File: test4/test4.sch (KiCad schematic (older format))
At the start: 2 parts, among them U1 74LS245, U2 74LS245

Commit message: playing with schematic symbol editor
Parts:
- added U?: test1, symbol test1
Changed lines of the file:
@@
 LIBS:contrib
 LIBS:valves
+LIBS:test1
+LIBS:test4-cache
 EELAYER 25 0
 EELAYER END
@@
 	4950 5050 4950 4850
 Connection ~ 4950 4850
+$Comp
+L test1 U?
+U 1 1 5672C530
+P 7400 1600
+F 0 "U?" H 7400 1600 60  0000 C CNN
+F 1 "test1" H 7400 1600 60  0000 C CNN
+F 2 "" H 7400 1600 60  0000 C CNN
+F 3 "" H 7400 1600 60  0000 C CNN
+	1    7400 1600
+	1    0    0    -1
+$EndComp
 $EndSCHEMATC

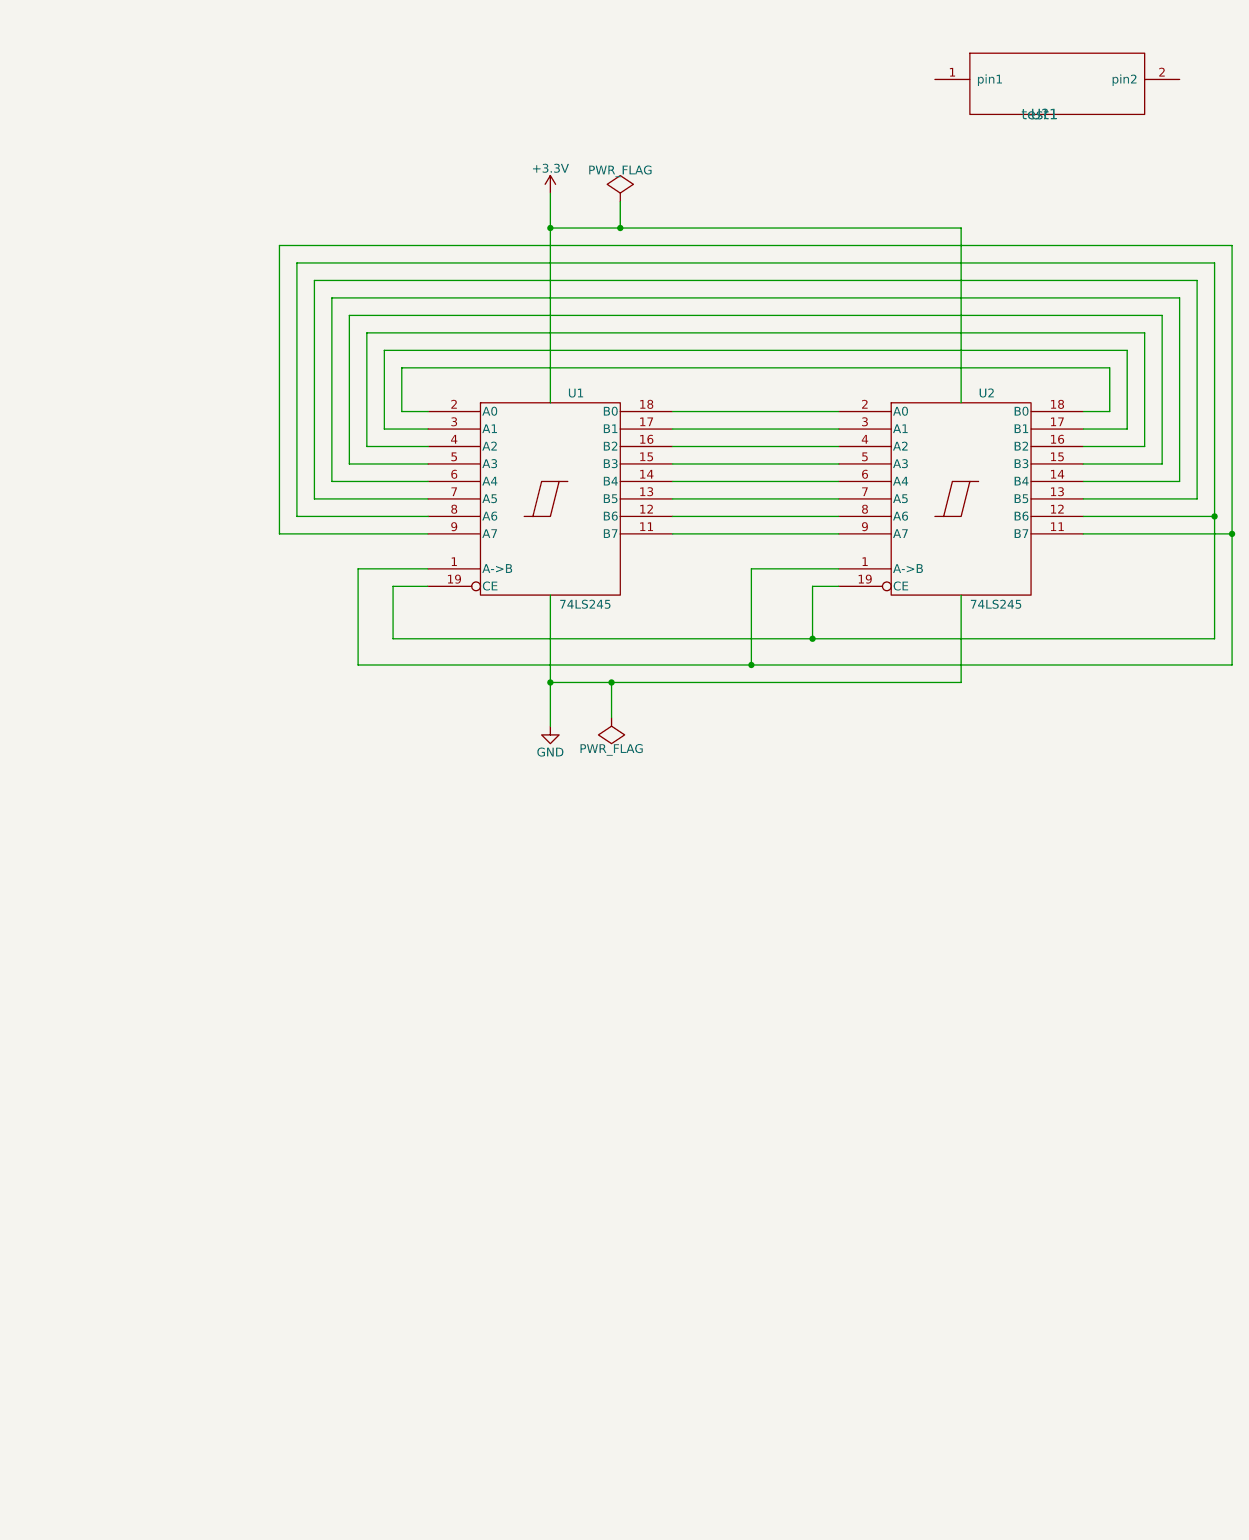
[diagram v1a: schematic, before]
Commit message: adding schematic pseudo-symbol for AD9361
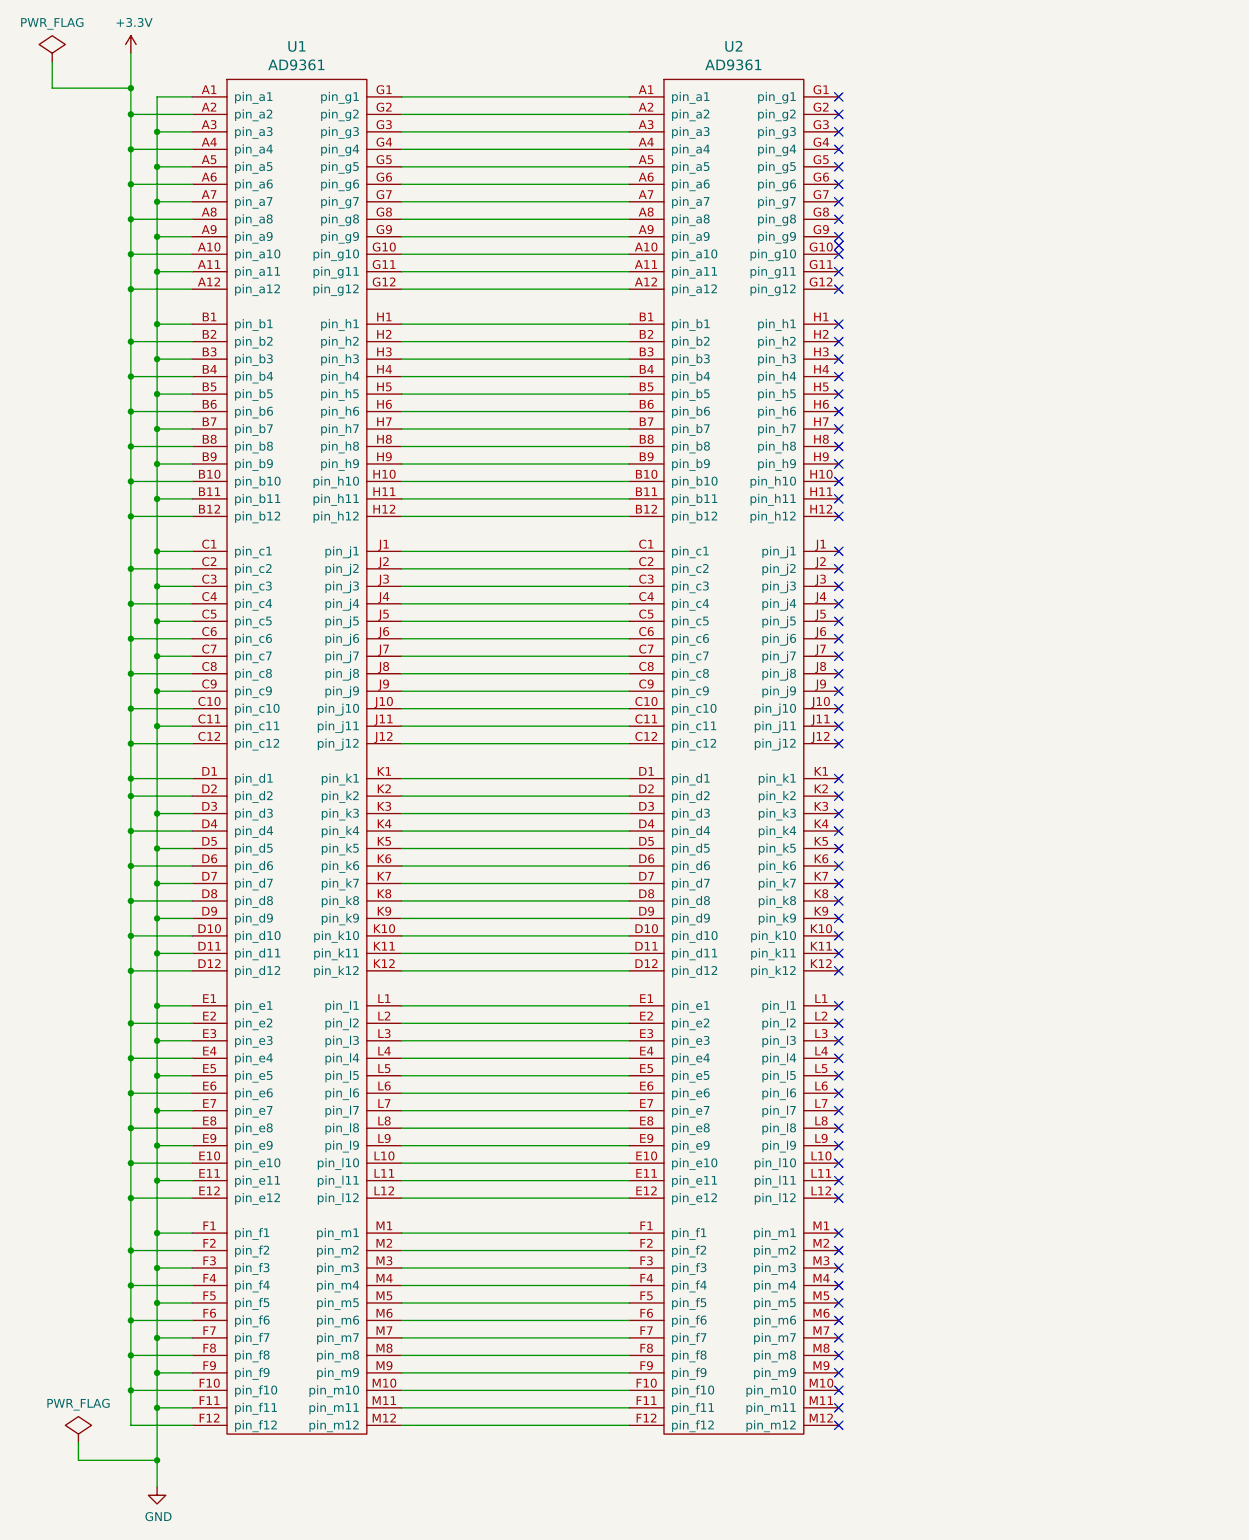
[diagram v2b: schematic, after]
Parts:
- removed U1, U2: 74LS245, SMD_Packages:SSOP-20, symbol 74LS245
- removed U?: test1, symbol test1
- added U1, U2: AD9361, footprintlib:AD9361, symbol AD9361
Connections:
- net +3V3: now also U1.A10 (pin_a10), U1.A12 (pin_a12), U1.A2 (pin_a2), U1.A4 (pin_a4), U1.A6 (pin_a6), U1.A8 (pin_a8), U1.B10 (pin_b10), U1.B12 (pin_b12), U1.B2 (pin_b2), U1.B4 (pin_b4), U1.B6 (pin_b6), U1.B8 (pin_b8), U1.C10 (pin_c10), U1.C12 (pin_c12), U1.C2 (pin_c2), U1.C4 (pin_c4), U1.C6 (pin_c6), U1.C8 (pin_c8), U1.D1 (pin_d1), U1.D10 (pin_d10), U1.D12 (pin_d12), U1.D2 (pin_d2), U1.D4 (pin_d4), U1.D6 (pin_d6), U1.D8 (pin_d8), U1.E10 (pin_e10), U1.E12 (pin_e12), U1.E2 (pin_e2), U1.E4 (pin_e4), U1.E6 (pin_e6), U1.E8 (pin_e8), U1.F10 (pin_f10), U1.F12 (pin_f12), U1.F2 (pin_f2), U1.F4 (pin_f4), U1.F6 (pin_f6), U1.F8 (pin_f8)
- net GND: now also U1.A1 (pin_a1), U1.A11 (pin_a11), U1.A3 (pin_a3), U1.A5 (pin_a5), U1.A7 (pin_a7), U1.A9 (pin_a9), U1.B1 (pin_b1), U1.B11 (pin_b11), U1.B3 (pin_b3), U1.B5 (pin_b5), U1.B7 (pin_b7), U1.B9 (pin_b9), U1.C1 (pin_c1), U1.C11 (pin_c11), U1.C3 (pin_c3), U1.C5 (pin_c5), U1.C7 (pin_c7), U1.C9 (pin_c9), U1.D11 (pin_d11), U1.D3 (pin_d3), U1.D5 (pin_d5), U1.D7 (pin_d7), U1.D9 (pin_d9), U1.E1 (pin_e1), U1.E11 (pin_e11), U1.E3 (pin_e3), U1.E5 (pin_e5), U1.E7 (pin_e7), U1.E9 (pin_e9), U1.F1 (pin_f1), U1.F11 (pin_f11), U1.F3 (pin_f3), U1.F5 (pin_f5), U1.F7 (pin_f7), U1.F9 (pin_f9)
- new net: U1.G1 (pin_g1), U2.A1 (pin_a1)
- new net: U1.G10 (pin_g10), U2.A10 (pin_a10)
- new net: U1.G11 (pin_g11), U2.A11 (pin_a11)
- new net: U1.G12 (pin_g12), U2.A12 (pin_a12)
- new net: U1.G2 (pin_g2), U2.A2 (pin_a2)
- new net: U1.G3 (pin_g3), U2.A3 (pin_a3)
- new net: U1.G4 (pin_g4), U2.A4 (pin_a4)
- new net: U1.G5 (pin_g5), U2.A5 (pin_a5)
- new net: U1.G6 (pin_g6), U2.A6 (pin_a6)
- new net: U1.G7 (pin_g7), U2.A7 (pin_a7)
- new net: U1.G8 (pin_g8), U2.A8 (pin_a8)
- new net: U1.G9 (pin_g9), U2.A9 (pin_a9)
- new net: U1.H1 (pin_h1), U2.B1 (pin_b1)
- new net: U1.H10 (pin_h10), U2.B10 (pin_b10)
- new net: U1.H11 (pin_h11), U2.B11 (pin_b11)
- new net: U1.H12 (pin_h12), U2.B12 (pin_b12)
- new net: U1.H2 (pin_h2), U2.B2 (pin_b2)
- new net: U1.H3 (pin_h3), U2.B3 (pin_b3)
- new net: U1.H4 (pin_h4), U2.B4 (pin_b4)
- new net: U1.H5 (pin_h5), U2.B5 (pin_b5)
- new net: U1.H6 (pin_h6), U2.B6 (pin_b6)
- new net: U1.H7 (pin_h7), U2.B7 (pin_b7)
- new net: U1.H8 (pin_h8), U2.B8 (pin_b8)
- new net: U1.H9 (pin_h9), U2.B9 (pin_b9)
- new net: U1.J1 (pin_j1), U2.C1 (pin_c1)
- new net: U1.J10 (pin_j10), U2.C10 (pin_c10)
- new net: U1.J11 (pin_j11), U2.C11 (pin_c11)
- new net: U1.J12 (pin_j12), U2.C12 (pin_c12)
- new net: U1.J2 (pin_j2), U2.C2 (pin_c2)
- new net: U1.J3 (pin_j3), U2.C3 (pin_c3)
- new net: U1.J4 (pin_j4), U2.C4 (pin_c4)
- new net: U1.J5 (pin_j5), U2.C5 (pin_c5)
- new net: U1.J6 (pin_j6), U2.C6 (pin_c6)
- new net: U1.J7 (pin_j7), U2.C7 (pin_c7)
- new net: U1.J8 (pin_j8), U2.C8 (pin_c8)
- new net: U1.J9 (pin_j9), U2.C9 (pin_c9)
- new net: U1.K1 (pin_k1), U2.D1 (pin_d1)
- new net: U1.K10 (pin_k10), U2.D10 (pin_d10)
- new net: U1.K11 (pin_k11), U2.D11 (pin_d11)
- new net: U1.K12 (pin_k12), U2.D12 (pin_d12)
- new net: U1.K2 (pin_k2), U2.D2 (pin_d2)
- new net: U1.K3 (pin_k3), U2.D3 (pin_d3)
- new net: U1.K4 (pin_k4), U2.D4 (pin_d4)
- new net: U1.K5 (pin_k5), U2.D5 (pin_d5)
- new net: U1.K6 (pin_k6), U2.D6 (pin_d6)
- new net: U1.K7 (pin_k7), U2.D7 (pin_d7)
- new net: U1.K8 (pin_k8), U2.D8 (pin_d8)
- new net: U1.K9 (pin_k9), U2.D9 (pin_d9)
- new net: U1.L1 (pin_l1), U2.E1 (pin_e1)
- new net: U1.L10 (pin_l10), U2.E10 (pin_e10)
- new net: U1.L11 (pin_l11), U2.E11 (pin_e11)
- new net: U1.L12 (pin_l12), U2.E12 (pin_e12)
- new net: U1.L2 (pin_l2), U2.E2 (pin_e2)
- new net: U1.L3 (pin_l3), U2.E3 (pin_e3)
- new net: U1.L4 (pin_l4), U2.E4 (pin_e4)
- new net: U1.L5 (pin_l5), U2.E5 (pin_e5)
- new net: U1.L6 (pin_l6), U2.E6 (pin_e6)
- new net: U1.L7 (pin_l7), U2.E7 (pin_e7)
- new net: U1.L8 (pin_l8), U2.E8 (pin_e8)
- new net: U1.L9 (pin_l9), U2.E9 (pin_e9)
- new net: U1.M1 (pin_m1), U2.F1 (pin_f1)
- new net: U1.M10 (pin_m10), U2.F10 (pin_f10)
- new net: U1.M11 (pin_m11), U2.F11 (pin_f11)
- new net: U1.M12 (pin_m12), U2.F12 (pin_f12)
- new net: U1.M2 (pin_m2), U2.F2 (pin_f2)
- new net: U1.M3 (pin_m3), U2.F3 (pin_f3)
- new net: U1.M4 (pin_m4), U2.F4 (pin_f4)
- new net: U1.M5 (pin_m5), U2.F5 (pin_f5)
- new net: U1.M6 (pin_m6), U2.F6 (pin_f6)
- new net: U1.M7 (pin_m7), U2.F7 (pin_f7)
- new net: U1.M8 (pin_m8), U2.F8 (pin_f8)
- new net: U1.M9 (pin_m9), U2.F9 (pin_f9)
- no-connect marks 0 -> 73
